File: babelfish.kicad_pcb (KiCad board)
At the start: 4 copper layers, 44.5 x 37.2 mm, 50 parts, among them J1 USB_C_Receptacle_USB2.0, J2 Conn_01x02, J3 SWD, J4 USB_C_Receptacle_USB2.0, J5 IO_A, J6 IO_B, U1 NCP1117-3.3_SOT223, U2 W25Q128JVS, U3 RP2040, U4 WS3232ECY, Y1 X322512MSB4SI

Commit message: updates
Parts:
- added C22: 10u, Capacitor_SMD:C_0805_2012Metric, F.Cu at (120.3, 106.2)
- added FB1: FerriteBead_Small, Inductor_SMD:L_0805_2012Metric, F.Cu at (123.7, 105.3)
- added J7: USB_A, RP2040_minimal:USB-A-TH__USB-AF-90, F.Cu at (128.8, 101.8)
- added Q1: ~, Package_TO_SOT_SMD:SOT-23-3, F.Cu at (103.5, 124.6)
- added Q2: ~, Package_TO_SOT_SMD:SOT-23-3, F.Cu at (103.5, 128.2)
- added Q3: ~, Package_TO_SOT_SMD:SOT-23-3, F.Cu at (103.5, 131.8)
- added Q4: ~, Package_TO_SOT_SMD:SOT-23-3, F.Cu at (103.5, 135.4)
- added R12: 10k, Resistor_SMD:R_0402_1005Metric, F.Cu at (106.5, 125.5)
- added R13: 10k, Resistor_SMD:R_0402_1005Metric, F.Cu at (100.6, 124.2)
- added R14: 10k, Resistor_SMD:R_0402_1005Metric, F.Cu at (106.5, 127.7)
- added R15: 10k, Resistor_SMD:R_0402_1005Metric, F.Cu at (100.6, 126.7)
- added R16: 10k, Resistor_SMD:R_0402_1005Metric, F.Cu at (106.5, 132.7)
- added R17: 10k, Resistor_SMD:R_0402_1005Metric, F.Cu at (100.6, 131.4)
- added R18: 10k, Resistor_SMD:R_0402_1005Metric, F.Cu at (106.5, 134.9)
- added R19: 10k, Resistor_SMD:R_0402_1005Metric, F.Cu at (100.6, 133.9)
- J1: value USB_C_Receptacle_USB2.0 -> TYPE-C-31-M-12
- J4: value USB_C_Receptacle_USB2.0 -> Shifter Power; footprint Connector_USB:USB_C_Receptacle_HRO_TYPE-C-31-M-12 -> Connector_PinHeader_2.54mm:PinHeader_2x03_P2.54mm_Vertical
- R10, R9: value 5.1K -> 15k; footprint Resistor_SMD:R_0402_1005Metric -> Capacitor_SMD:C_0402_1005Metric
- R11, R5: value 27 -> 22
- moved J3 36.2 mm to (129.0, 87.8)
- moved J4 23.9 mm to (114.5, 126.1), turned to 0 degrees
- moved H3 14.9 mm to (135.3, 81.1)
- moved H2 14.9 mm to (135.3, 112.0)
- moved R9 9.41 mm to (123.9, 100.6), turned to 180 degrees
- moved R10 8.45 mm to (123.9, 102.9), turned to 180 degrees
- moved H1 7.82 mm to (86.2, 114.0)
- moved H4 2.18 mm to (86.2, 79.5)
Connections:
- J5 pad 2: /GPIO6 -> /U1_RX_CH
- J5 pad 4: /GPIO2 -> /U1_TX_CH
- J5 pad 6: /GPIO20 -> /U0_RX_CH
- J5 pad 8: /GPIO21 -> /U0_TX_CH
- R10 pad 1: GND -> /USB2_D-
- R10 pad 2: Net-(J4-CC2) -> GND
- R11 pad 2: /GPIO17 -> /GPIO15
- R5 pad 2: /GPIO16 -> /GPIO14
- R8 pad 1: +3V3 -> /RUN
- R8 pad 2: /RUN -> +3V3
- R9 pad 1: GND -> /USB2_D+
- R9 pad 2: Net-(J4-CC1) -> GND
- U3 pad 27: /GPIO16 -> /U0_TX_C
- U3 pad 28: /GPIO17 -> /U0_RX_C
- U3 pad 31: /GPIO20 -> /U1_TX_C
- U3 pad 32: /GPIO21 -> /U1_RX_C
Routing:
- net /GPIO21: track 42.0 -> 0.00 mm, vias 1 -> 0
- net /GPIO20: track 38.9 -> 0.00 mm, vias 1 -> 0
- net /SWD: track 29.1 -> 0.00 mm, vias 2 -> 0
- net /SWCLK: track 28.4 -> 0.00 mm, vias 2 -> 0
- net /GPIO2: track 24.3 -> 0.00 mm
- net +3.3V: track 0.00 -> 24.1 mm
- net /GPIO6: track 20.3 -> 0.00 mm
- net /USB2_D-: track 7.57 -> 17.6 mm
- net /USB2_D+: track 7.84 -> 17.4 mm
- net /GPIO16: track 4.69 -> 0.00 mm
- net VBUS: track 14.1 -> 9.38 mm
- net GND: track 26.5 -> 21.9 mm
- net /GPIO17: track 3.88 -> 0.00 mm
- net Net-(J7-VBUS): track 0.00 -> 2.68 mm
- net Net-(J4-CC2): track 2.28 -> 0.00 mm
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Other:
- board size 44.5 x 37.2 mm -> 57.7 x 47.7 mm

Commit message: rev 0.1
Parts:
- removed C18, C19, C20, C21: 0.1uf, Capacitor_SMD:C_0402_1005Metric
- removed D2: 1N5819WS, Diode_SMD:D_SOD-323
- removed J1: TYPE-C-31-M-12, Connector_USB:USB_C_Receptacle_HRO_TYPE-C-31-M-12
- removed J2: Conn_01x02, Connector_PinHeader_2.54mm:PinHeader_1x02_P2.54mm_Vertical
- removed J6: IO_B, Connector_PinHeader_2.54mm:PinHeader_2x05_P2.54mm_Horizontal
- removed Y1: X322512MSB4SI, Crystal:Crystal_SMD_3225-4Pin_3.2x2.5mm
- added R20: 1k, Resistor_SMD:R_0402_1005Metric, F.Cu at (106.5, 94.3)
- added SW1: K2-1156SP-D5SW-05, lcsc:SW-SMD_4P-L6.3-W6.2-P4.00-LS9.4-TL, F.Cu at (119.1, 102.0)
- added X1: X322512MSB4SI, lcsc:OSC-SMD_4P-L3.2-W2.5-BL, F.Cu at (104.5, 97.1)
- added kibuzzard-644F3679: G***, kibuzzard-644F3679, F.Cu at (95.0, 104.5)
- added kibuzzard-644F39EB: G***, kibuzzard-644F39EB, F.Cu at (131.4, 77.5)
- added kibuzzard-644F3A2B: G***, kibuzzard-644F3A2B, F.Cu at (134.6, 80.9)
- C2, C3: value 32p -> 30p
- Q1: value ~ -> BSS138
- R1, R10, R11, R2, R3, R4, R5, R9: footprint Capacitor_SMD:C_0402_1005Metric -> Resistor_SMD:R_0402_1005Metric
- U4: value WS3232ECY -> GT-USB-7010ASV; footprint Package_SO:TSSOP-16_4.4x5mm_P0.65mm -> lcsc:USB-C-SMD_G-SWITCH_GT-USB-7010ASV
- moved Q4 48.3 mm to (89.4, 89.2), turned to 180 degrees
- moved R18 47.8 mm to (92.0, 89.3), turned to 90 degrees
- moved R19 46.4 mm to (86.7, 89.7), turned to 90 degrees
- moved R16 42.6 mm to (92.0, 92.7)
- moved R17 41.6 mm to (86.7, 92.1), turned to -90 degrees
- moved Q3 41.6 mm to (89.4, 92.7), turned to 180 degrees
- moved U4 35.5 mm to (110.6, 74.3)
- moved Q2 35.0 mm to (89.4, 96.2), turned to 180 degrees
- moved R14 34.7 mm to (92.0, 96.2), turned to 90 degrees
- moved R15 33.1 mm to (86.7, 96.7), turned to 90 degrees
- moved R12 29.5 mm to (92.0, 99.7)
- moved Q1 28.6 mm to (89.4, 99.7), turned to 180 degrees
- moved R13 28.6 mm to (86.7, 99.2), turned to -90 degrees
- moved J4 24.9 mm to (103.7, 103.7), turned to 90 degrees
- moved J3 16.4 mm to (122.0, 73.0)
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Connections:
- net Net-(D3-A) renamed /VCC_IN
- C2 pad 1: /XIN -> Net-(X1-OSC1)
- C2 pad 2: GND -> Net-(C2-Pad2)
- C3 pad 1: /XOUT -> Net-(X1-OSC2)
- C3 pad 2: GND -> /XIN
- J3 pad 3: /SWD -> GND
- J3 pad 4: GND -> /SWD
- J4 pad 1: Net-(J4-Pin_1) -> /SH_REF
- J4 pad 3: Net-(J4-Pin_1) -> /SH_REF
- J4 pad 5: Net-(J4-Pin_1) -> /SH_REF
- J4 pad 6: +3V3 -> VCC
- Q1 pad 1: /U0_TX_CH -> +3V3
- Q1 pad 2: +3.3V -> /U0_TX_B
- Q1 pad 3: /U0_TX_C -> /U0_TX_CH
- Q2 pad 1: /U0_RX_CH -> +3V3
- Q2 pad 2: +3.3V -> /U0_RX_B
- Q2 pad 3: /U0_RX_C -> /U0_RX_CH
- Q3 pad 1: /U1_TX_CH -> +3V3
- Q3 pad 2: +3.3V -> /U1_TX_B
- Q3 pad 3: /U1_TX_C -> /U1_TX_CH
- Q4 pad 1: /U1_RX_CH -> +3V3
- Q4 pad 2: +3.3V -> /U1_RX_B
- Q4 pad 3: /U1_RX_C -> /U1_RX_CH
- R11 pad 2: /GPIO15 -> /GPIO19
- R12 pad 1: +3.3V -> +3V3
- R12 pad 2: /U0_TX_C -> /U0_TX_B
- R13 pad 1: unconnected-(R13-Pad1) -> /SH_REF
- R14 pad 1: +3.3V -> +3V3
- R14 pad 2: /U0_RX_C -> /U0_RX_B
- R15 pad 1: unconnected-(R15-Pad1) -> /SH_REF
- R16 pad 1: +3.3V -> +3V3
- R16 pad 2: /U1_TX_C -> /U1_TX_B
- R17 pad 1: unconnected-(R17-Pad1) -> /SH_REF
- R18 pad 1: +3.3V -> +3V3
- R18 pad 2: /U1_RX_C -> /U1_RX_B
- R19 pad 1: unconnected-(R19-Pad1) -> /SH_REF
- R5 pad 2: /GPIO14 -> /GPIO18
- R6 pad 1: GND -> Net-(U4-CC1)
- R6 pad 2: Net-(J1-CC1) -> GND
- R7 pad 1: GND -> Net-(U4-CC2)
- R7 pad 2: Net-(J1-CC2) -> GND
- U4 pad 1: Net-(U4-C1+) -> GND
- U4 pad 2: Net-(U4-V+) -> GND
- U4 pad 3: Net-(U4-C1-) -> GND
- U4 pad 4: Net-(U4-C2+) -> GND
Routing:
- net +3V3: track 42.2 -> 163.5 mm, vias 0 -> 8
- net GND: track 21.9 -> 72.5 mm, vias 10 -> 31
- net VCC: track 33.8 -> 76.9 mm, vias 2 -> 3
- net VBUS: track 9.38 -> 51.0 mm, vias 0 -> 2
- net /SH_REF: track 0.00 -> 37.0 mm
- net /SWD: track 0.00 -> 32.3 mm, vias 0 -> 1
- net /~{USB_BOOT}: track 14.6 -> 46.1 mm
- net /SWCLK: track 0.00 -> 28.1 mm, vias 0 -> 1
- net /U0_TX_CH: track 1.73 -> 27.2 mm
- net +3.3V: track 24.1 -> 0.00 mm
- net /U0_RX_CH: track 1.75 -> 20.8 mm
- net /U0_232_TX: track 13.5 -> 0.00 mm, vias 2 -> 0
- net /U1_TX_CH: track 1.73 -> 14.9 mm
- net /U0_232_RX: track 12.8 -> 0.00 mm, vias 2 -> 0
- net /XIN: track 11.0 -> 2.84 mm
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- added copper zone on B.Cu, net (none)
- added copper zone on F.Cu, net +3V3
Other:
- board size 57.7 x 47.7 mm -> 57 x 38.7 mm
- rule pad_to_mask_clearance: 0.051 -> 0
- board text added: "@SH"
- board text added: "BOOT"
- board text added: "DBG"
- board text added: "GND"
- board text added: "NC 5V VCC"
- board text added: "U0"
- board text added: "U1"
- board text added: "VCC"

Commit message: rev2, pre review
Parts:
- removed J4: Shifter Power, Connector_PinHeader_2.54mm:PinHeader_2x03_P2.54mm_Vertical
- removed kibuzzard-644F3A2B: G***, kibuzzard-644F3A2B
- added C18: 4u7, Capacitor_SMD:C_0603_1608Metric, F.Cu at (132.7, 85.2)
- added C19: 10u, Capacitor_SMD:C_0805_2012Metric, F.Cu at (127.8, 88.6)
- added D2: Red, LED_SMD:LED_0603_1608Metric, F.Cu at (97.4, 97.8)
- added D4: Red, LED_SMD:LED_0603_1608Metric, F.Cu at (97.4, 99.3)
- added D5: Blue, LED_SMD:LED_0603_1608Metric, F.Cu at (97.4, 100.9)
- added D6: 40V/5A, Diode_SMD:D_SOD-323, F.Cu at (127.8, 86.6)
- added L1: 4u7, Inductor_SMD:L_1008_2520Metric, F.Cu at (129.6, 83.6)
- added R21: 68, Resistor_SMD:R_0603_1608Metric, F.Cu at (100.5, 97.8)
- added R22: 68, Resistor_SMD:R_0603_1608Metric, F.Cu at (100.5, 99.3)
- added R23: 68, Resistor_SMD:R_0603_1608Metric, F.Cu at (100.5, 100.9)
- added R24: 47k, Resistor_SMD:R_0603_1608Metric, F.Cu at (128.2, 90.4)
- added R25: 15k, Resistor_SMD:R_0603_1608Metric, F.Cu at (131.8, 90.2)
- added R26: 10k, Resistor_SMD:R_0402_1005Metric, F.Cu at (134.2, 87.3)
- added U5: LGS6302, lcsc:SOT-23-5_L3.0-W1.6-P0.95-LS2.8-BL, F.Cu at (131.6, 87.7)
- J3: footprint Connector_PinHeader_2.54mm:PinHeader_1x04_P2.54mm_Vertical -> SnapEDA:490107670412
- SW1: value K2-1156SP-D5SW-05 -> K2-1836UQ-C3DW-06; footprint lcsc:SW-SMD_4P-L6.3-W6.2-P4.00-LS9.4-TL -> lcsc:SW-SMD_4P-L2.8-W2.4-P1.60-LS3.0
- U3: renamed from U1; value NCP1117-3.3_SOT223 -> AMS1117-3.3
- moved kibuzzard-644F39EB 34.4 mm to (107.4, 102.2)
- moved SW1 34.3 mm to (102.8, 71.8), turned to 0 degrees
- moved J7 9.51 mm to (120.9, 96.8), turned to 0 degrees
- moved C22 5.31 mm to (123.5, 89.5), turned to 180 degrees
- moved J3 4.39 mm to (126.3, 73.9), turned to 0 degrees
- moved R10 4.22 mm to (119.8, 93.5)
- moved R9 3.70 mm to (122.0, 93.5), turned to 0 degrees
- moved Q4 3.55 mm to (89.4, 92.7)
- moved R14 3.54 mm to (92.0, 99.7)
- moved Q2 3.54 mm to (89.4, 99.8)
- moved Q1 3.46 mm to (89.4, 96.2)
- moved R12 3.46 mm to (92.0, 96.3)
- moved R16 3.45 mm to (92.0, 89.2)
- moved Q3 3.45 mm to (89.4, 89.2)
- moved R18 3.40 mm to (92.0, 92.7)
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- renumbered U3 to U1
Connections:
- net Net-(C2-Pad2) renamed /OSC1R
- net Net-(X1-OSC1) renamed /OSC1
- net Net-(X1-OSC2) renamed /OSC2
- C22 pad 1: VBUS -> +5V
- FB1 pad 2: VBUS -> +5V
- J3 pad 2: /SWCLK -> /SWD
- J3 pad 4: /SWD -> /SWCLK
- R13 pad 1: /SH_REF -> /VCC_IN
- R15 pad 1: /SH_REF -> /VCC_IN
- R17 pad 1: /SH_REF -> /VCC_IN
- R19 pad 1: /SH_REF -> /VCC_IN
- U1 pad 13: /GPIO10 -> /LED_P_OK
- U1 pad 14: /GPIO11 -> /LED_AUX
- U1 pad 8: /GPIO6 -> /LED_PWR
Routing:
- net /SH_REF: track 37.0 -> 0.00 mm
- net VBUS: track 51.0 -> 14.3 mm, vias 2 -> 0
- net VCC: track 76.9 -> 43.7 mm, vias 3 -> 2
- net /VCC_IN: track 3.47 -> 36.5 mm, vias 0 -> 2
- net /~{USB_BOOT}: track 46.1 -> 15.0 mm, vias 2 -> 0
- net +1V1: track 5.62 -> 23.5 mm, vias 0 -> 4
- net /LED_PWR: track 0.00 -> 15.7 mm, vias 0 -> 2
- net /LED_AUX: track 0.00 -> 12.1 mm, vias 0 -> 2
- net /LED_P_OK: track 0.00 -> 11.9 mm, vias 0 -> 2
- net +5V: track 0.00 -> 9.13 mm
- net +3V3: track 163.5 -> 155.2 mm, vias 8 -> 10
- net Net-(J7-VBUS): track 2.68 -> 10.2 mm, vias 0 -> 1
- net GND: track 72.5 -> 65.2 mm, vias 31 -> 28
- net /USB2_D-: track 17.1 -> 10.8 mm
- net /USB2_D+: track 17.2 -> 12.1 mm
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- added copper zone on F.Cu, net +5V
- added copper zone on B.Cu, net GND
- removed copper zone on B.Cu, net (none)
- removed copper zone on In2.Cu, net +3V3
- removed copper zone on F.Cu, net GND
- removed copper zone on In1.Cu, net GND
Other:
- board size 57 x 38.7 mm -> 56 x 38.2 mm
- copper layers 4 -> 2
- board text added: "3v3"
- board text added: "A"
- board text added: "AUX"
- board text added: "B"
- board text added: "CLK"
- board text added: "OK"
- board text added: "PWR"
- board text added: "SWD"
- board text added: "Vcc"
- board text added: "rx"
- board text added: "tx"
- board text removed: "@SH"
- board text removed: "DBG"
- board text removed: "NC 5V VCC"
- board text removed: "Stackup: JLC3313"
- board text removed: "U0"
- board text removed: "U1"

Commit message: new
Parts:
- removed C18: 4u7, Capacitor_SMD:C_0603_1608Metric
- removed C19: 10u, Capacitor_SMD:C_0805_2012Metric
- removed D1, D3: 1N5819WS, Diode_SMD:D_SOD-323
- removed D6: 40V/5A, Diode_SMD:D_SOD-323
- removed L1: 4u7, Inductor_SMD:L_1008_2520Metric
- removed R24: 47k, Resistor_SMD:R_0603_1608Metric
- removed R25: 15k, Resistor_SMD:R_0603_1608Metric
- removed R26: 10k, Resistor_SMD:R_0402_1005Metric
- removed U5: LGS6302, lcsc:SOT-23-5_L3.0-W1.6-P0.95-LS2.8-BL
- added J1: Conn_02x02_Odd_Even, Connector_PinHeader_2.54mm:PinHeader_2x02_P2.54mm_Vertical, F.Cu at (73.0, 95.1)
- moved C1 5.22 mm to (123.5, 79.9), turned to 0 degrees
- moved C22 4.07 mm to (126.4, 92.3), turned to -90 degrees
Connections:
- C1 pad 1: VCC -> VBUS
- C22 pad 1: +5V -> VBUS
- FB1 pad 2: +5V -> VBUS
- R13 pad 1: /VCC_IN -> /VSH
- R15 pad 1: /VCC_IN -> /VSH
- R17 pad 1: /VCC_IN -> /VSH
- R19 pad 1: /VCC_IN -> /VSH
- U3 pad 3: VCC -> VBUS
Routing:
- net VBUS: track 14.3 -> 69.6 mm, vias 0 -> 2
- net VCC: track 43.7 -> 0.00 mm, vias 2 -> 0
- net +3V3: track 155.2 -> 139.9 mm, vias 10 -> 9
- net GND: track 65.2 -> 52.1 mm, vias 28 -> 25
- net +5V: track 9.13 -> 0.00 mm
- net /5V_FB: track 3.78 -> 0.00 mm
- net /5V_PRE: track 3.44 -> 0.00 mm
- net /5V_EN: track 1.63 -> 0.00 mm
- removed copper zone on F.Cu, net +5V

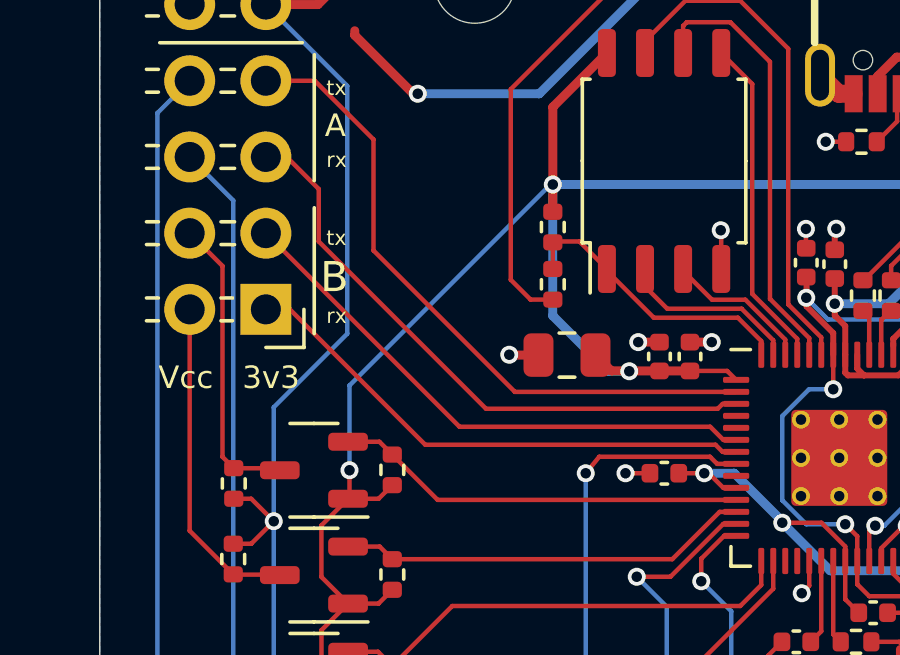
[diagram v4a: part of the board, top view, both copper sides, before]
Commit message: Moved files aroud. WIP new power section
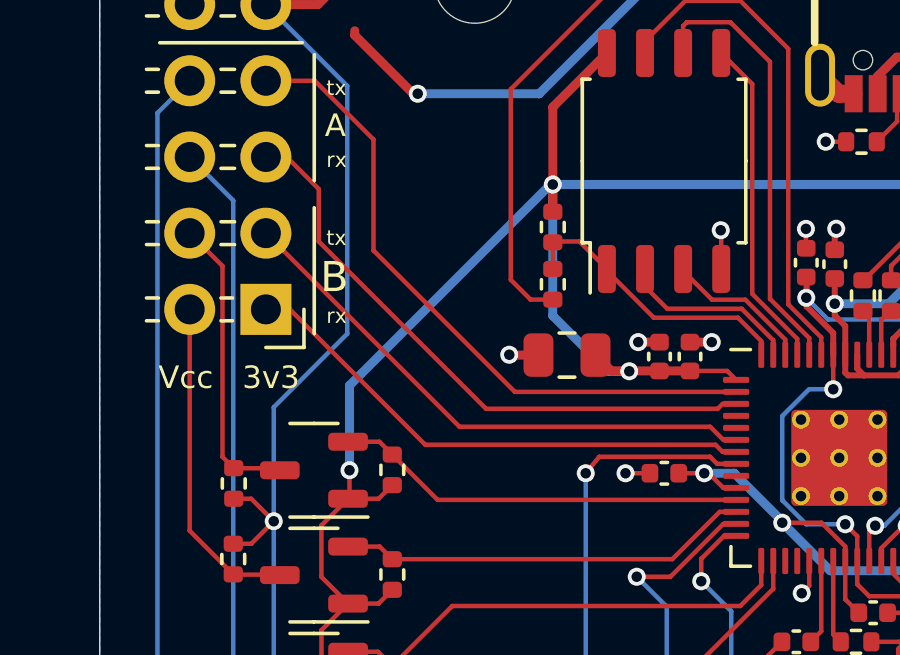
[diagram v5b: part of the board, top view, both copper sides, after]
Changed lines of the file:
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@@
   (segment (start 103.4 89.35) (end 102.4 89.35) (width 0.3) (layer "B.Cu") (net 5))
   (segment (start 97.275 79.725) (end 97.3521 79.725) (width 0.3) (layer "B.Cu") (net 5))
-  (segment (start 90.575 86.425) (end 90.575 89.25) (width 0.15) (layer "B.Cu") (net 5))
+  (segment (start 90.575 86.425) (end 90.575 89.25) (width 0.3) (layer "B.Cu") (net 5))
   (segment (start 97.3521 79.725) (end 108.975 79.725) (width 0.3) (layer "B.Cu") (net 5))
   (segment (start 106.6 92.6) (end 105 91) (width 0.3) (layer "B.Cu") (net 5))
@@
   (segment (start 113.3 89.85) (end 110.55 92.6) (width 0.3) (layer "B.Cu") (net 5))
   (segment (start 97.3521 79.725) (end 97.35 79.7271) (width 0.3) (layer "B.Cu") (net 5))
-  (segment (start 97.275 79.725) (end 90.575 86.425) (width 0.15) (layer "B.Cu") (net 5))
+  (segment (start 97.275 79.725) (end 90.575 86.425) (width 0.3) (layer "B.Cu") (net 5))
   (segment (start 113.3 93.6) (end 113.3 89.85) (width 0.15) (layer "B.Cu") (net 5))
   (segment (start 105 90.95) (end 103.4 89.35) (width 0.3) (layer "B.Cu") (net 5))
